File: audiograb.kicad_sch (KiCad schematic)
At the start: 8 parts, among them J2 USB_C_Receptacle_USB2.0_16P

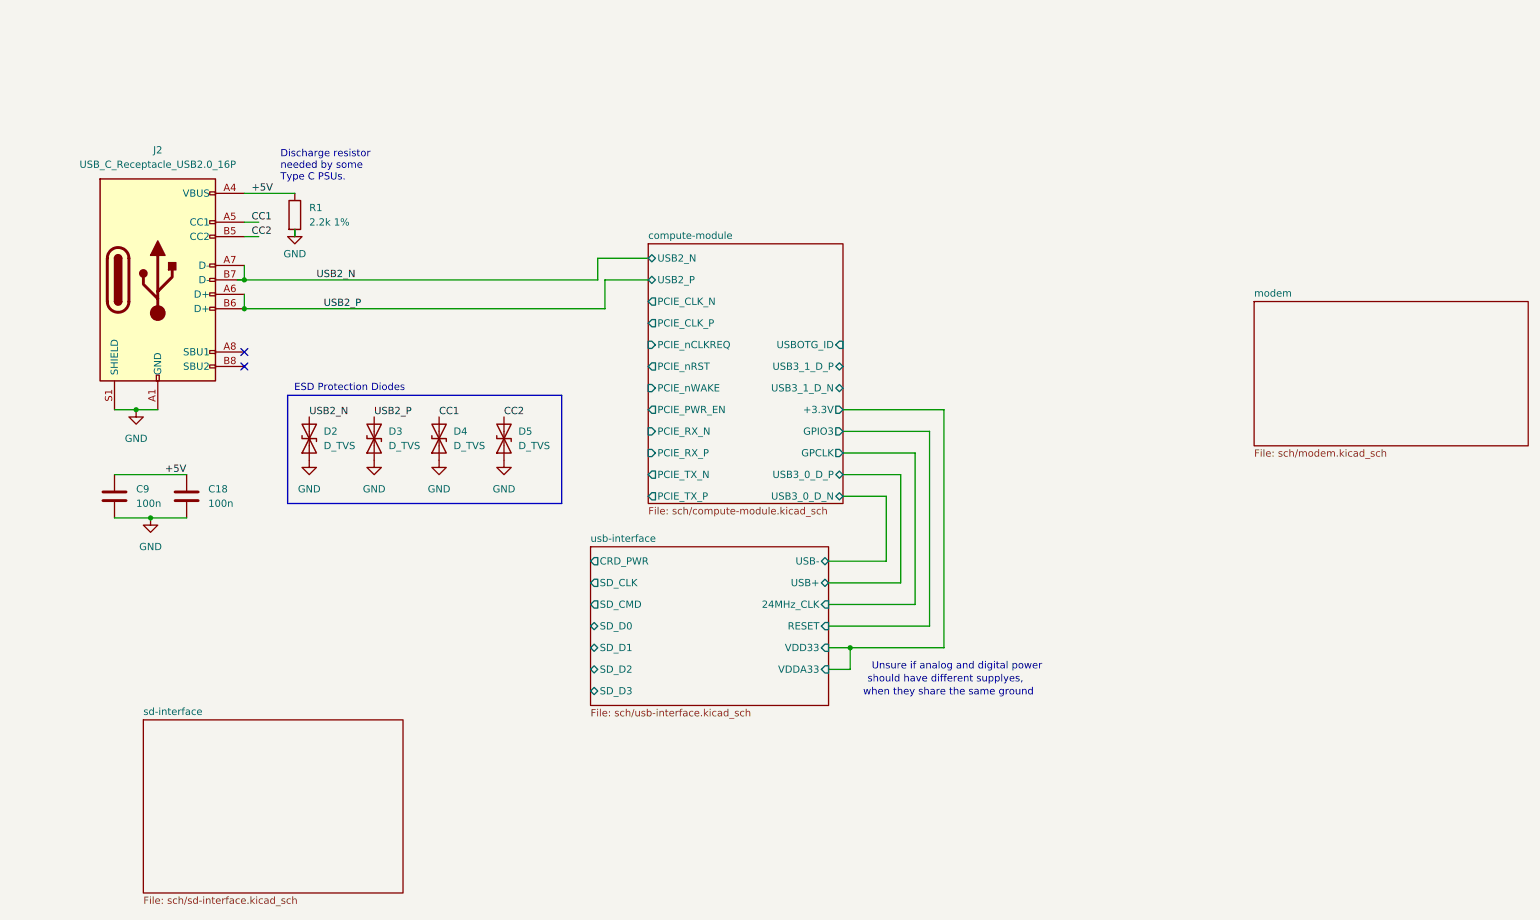
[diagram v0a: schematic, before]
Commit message: Connected pins between modem and CM5
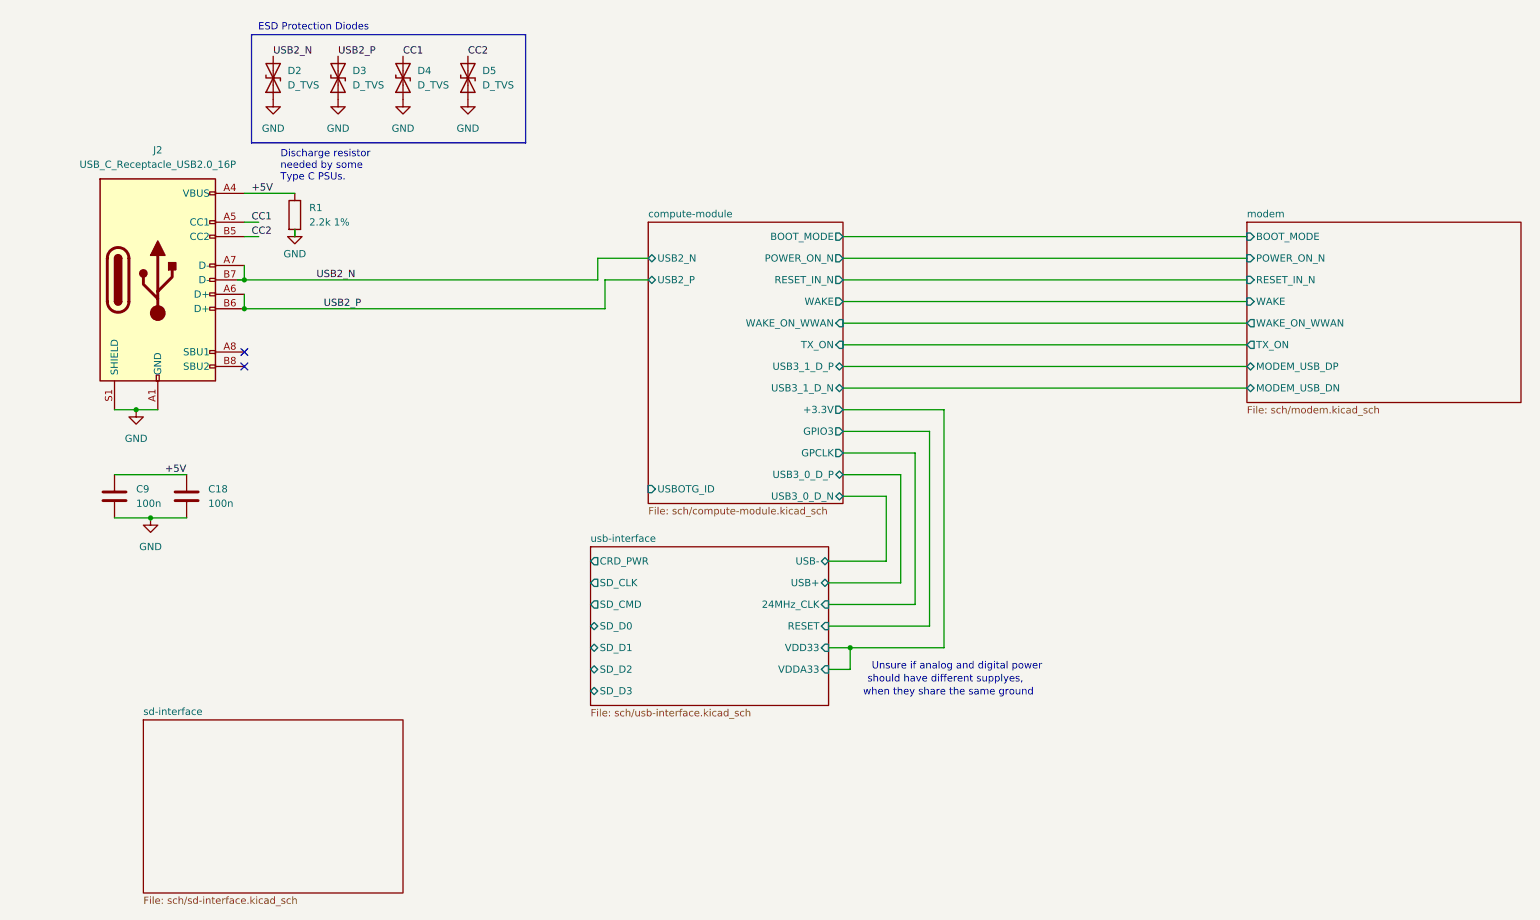
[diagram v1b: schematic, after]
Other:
- sheet compute-module ports: added BOOT_MODE, POWER_ON_N, RESET_IN_N, TX_ON, WAKE, WAKE_ON_WWAN; removed PCIE_CLK_N, PCIE_CLK_P, PCIE_PWR_EN, PCIE_RX_N, PCIE_RX_P, PCIE_TX_N, PCIE_TX_P, PCIE_nCLKREQ, PCIE_nRST, PCIE_nWAKE
- sheet modem ports: added BOOT_MODE, MODEM_USB_DN, MODEM_USB_DP, POWER_ON_N, RESET_IN_N, TX_ON, WAKE, WAKE_ON_WWAN; removed none
- moved on the sheet: D2, D3, D4, D5

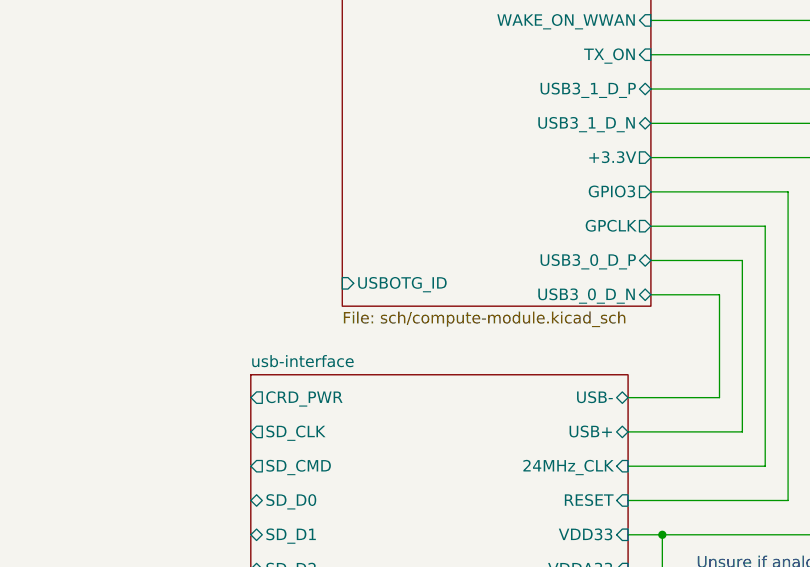
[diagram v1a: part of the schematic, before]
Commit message: Removed pin USBOTG
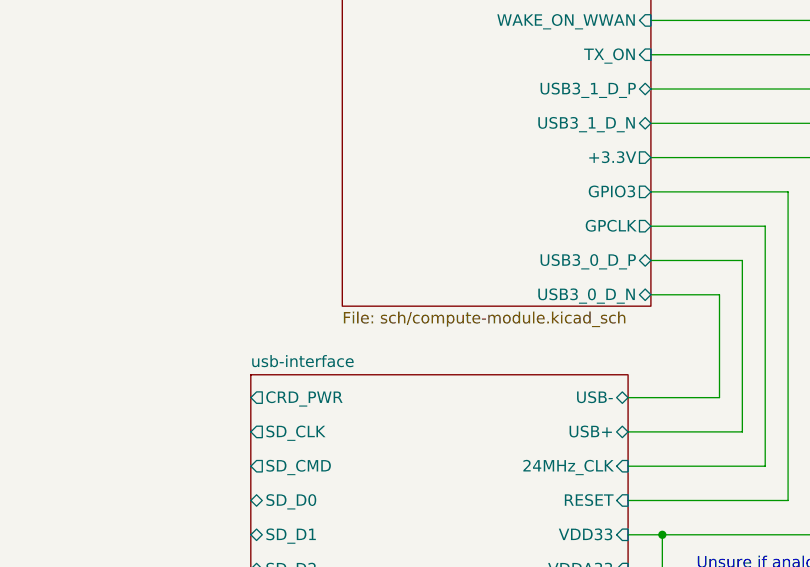
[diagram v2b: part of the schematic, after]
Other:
- sheet compute-module ports: added none; removed USBOTG_ID
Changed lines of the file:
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@@
-			)
-		)
-		(pin "USBOTG_ID" input
-			(at 123.19 96.52 180)
-			(effects
-				(font
-					(size 1.27 1.27)
-				)
-				(justify left)
 			)
 		)

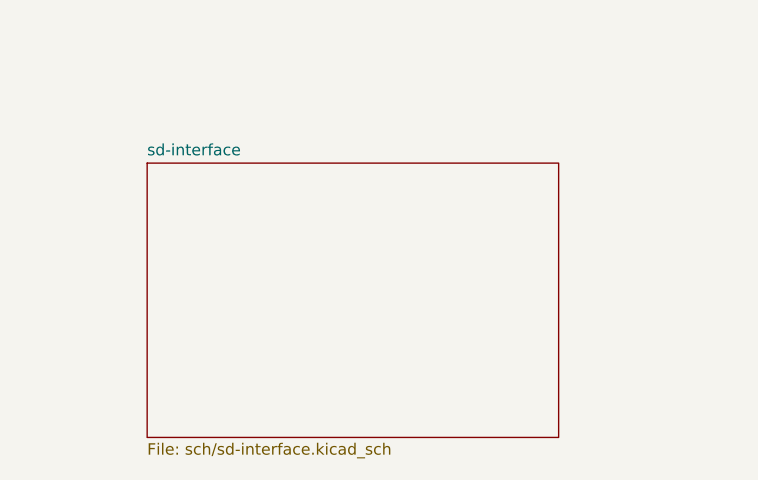
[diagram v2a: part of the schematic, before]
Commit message: added pins to sd_interface
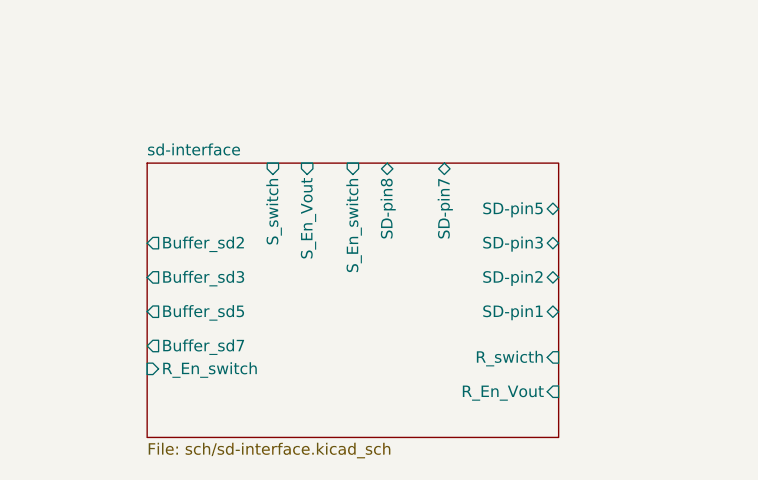
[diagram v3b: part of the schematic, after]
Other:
- sheet sd-interface ports: added Buffer_sd2, Buffer_sd3, Buffer_sd5, Buffer_sd7, R_En_Vout, R_En_switch, R_swicth, SD-pin1, SD-pin2, SD-pin3, SD-pin5, SD-pin7, SD-pin8, S_En_Vout, S_En_switch, S_switch; removed none
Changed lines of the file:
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@@
+			)
+		)
+		(pin "Buffer_sd2" output
+			(at 34.29 146.05 180)
+			(effects
+				(font
+					(size 1.27 1.27)
+				)
+				(justify left)
+			)
+		)
+		(pin "Buffer_sd3" output
+			(at 34.29 149.86 180)
+			(effects
+				(font
+					(size 1.27 1.27)
+				)
+				(justify left)
+			)
+		)
+		(pin "Buffer_sd5" output
+			(at 34.29 153.67 180)
+			(effects
+				(font
+					(size 1.27 1.27)
+				)
+				(justify left)
+			)
+		)
+		(pin "Buffer_sd7" output
+			(at 34.29 157.48 180)
+			(effects
+				(font
+					(size 1.27 1.27)
+				)
+				(justify left)
+			)
+		)
+		(pin "R_En_switch" input
+			(at 34.29 160.02 180)
+			(effects
+				(font
+					(size 1.27 1.27)
+				)
+				(justify left)
+			)
+		)
+		(pin "R_En_Vout" input
+			(at 80.01 162.56 0)
+			(effects
+				(font
+					(size 1.27 1.27)
+				)
+				(justify right)
+			)
+		)
+		(pin "R_swicth" input
+			(at 80.01 158.75 0)
+			(effects
+				(font
+					(size 1.27 1.27)
+				)
+				(justify right)
+			)
+		)
+		(pin "SD-pin1" bidirectional
+			(at 80.01 153.67 0)
+			(effects
+				(font
+					(size 1.27 1.27)
+				)
+				(justify right)
+			)
+		)
+		(pin "SD-pin2" bidirectional
+			(at 80.01 149.86 0)
+			(effects
+				(font
+					(size 1.27 1.27)
+				)
+				(justify right)
+			)
+		)
+		(pin "SD-pin3" bidirectional
+			(at 80.01 146.05 0)
+			(effects
+				(font
+					(size 1.27 1.27)
+				)
+				(justify right)
+			)
+		)
+		(pin "SD-pin5" bidirectional
+			(at 80.01 142.24 0)
+			(effects
+				(font
+					(size 1.27 1.27)
+				)
+				(justify right)
+			)
+		)
+		(pin "SD-pin7" bidirectional
+			(at 67.31 137.16 90)
+			(effects
+				(font
+					(size 1.27 1.27)
+				)
+				(justify right)
+			)
+		)
+		(pin "SD-pin8" bidirectional
+			(at 60.96 137.16 90)
+			(effects
+				(font
+					(size 1.27 1.27)
+				)
+				(justify right)
+			)
+		)
+		(pin "S_En_switch" input
+			(at 57.15 137.16 90)
+			(effects
+				(font
+					(size 1.27 1.27)
+				)
+				(justify right)
+			)
+		)
+		(pin "S_En_Vout" input
+			(at 52.07 137.16 90)
+			(effects
+				(font
+					(size 1.27 1.27)
+				)
+				(justify right)
+			)
+		)
+		(pin "S_switch" input
+			(at 48.26 137.16 90)
+			(effects
+				(font
+					(size 1.27 1.27)
+				)
+				(justify right)
 			)
 		)

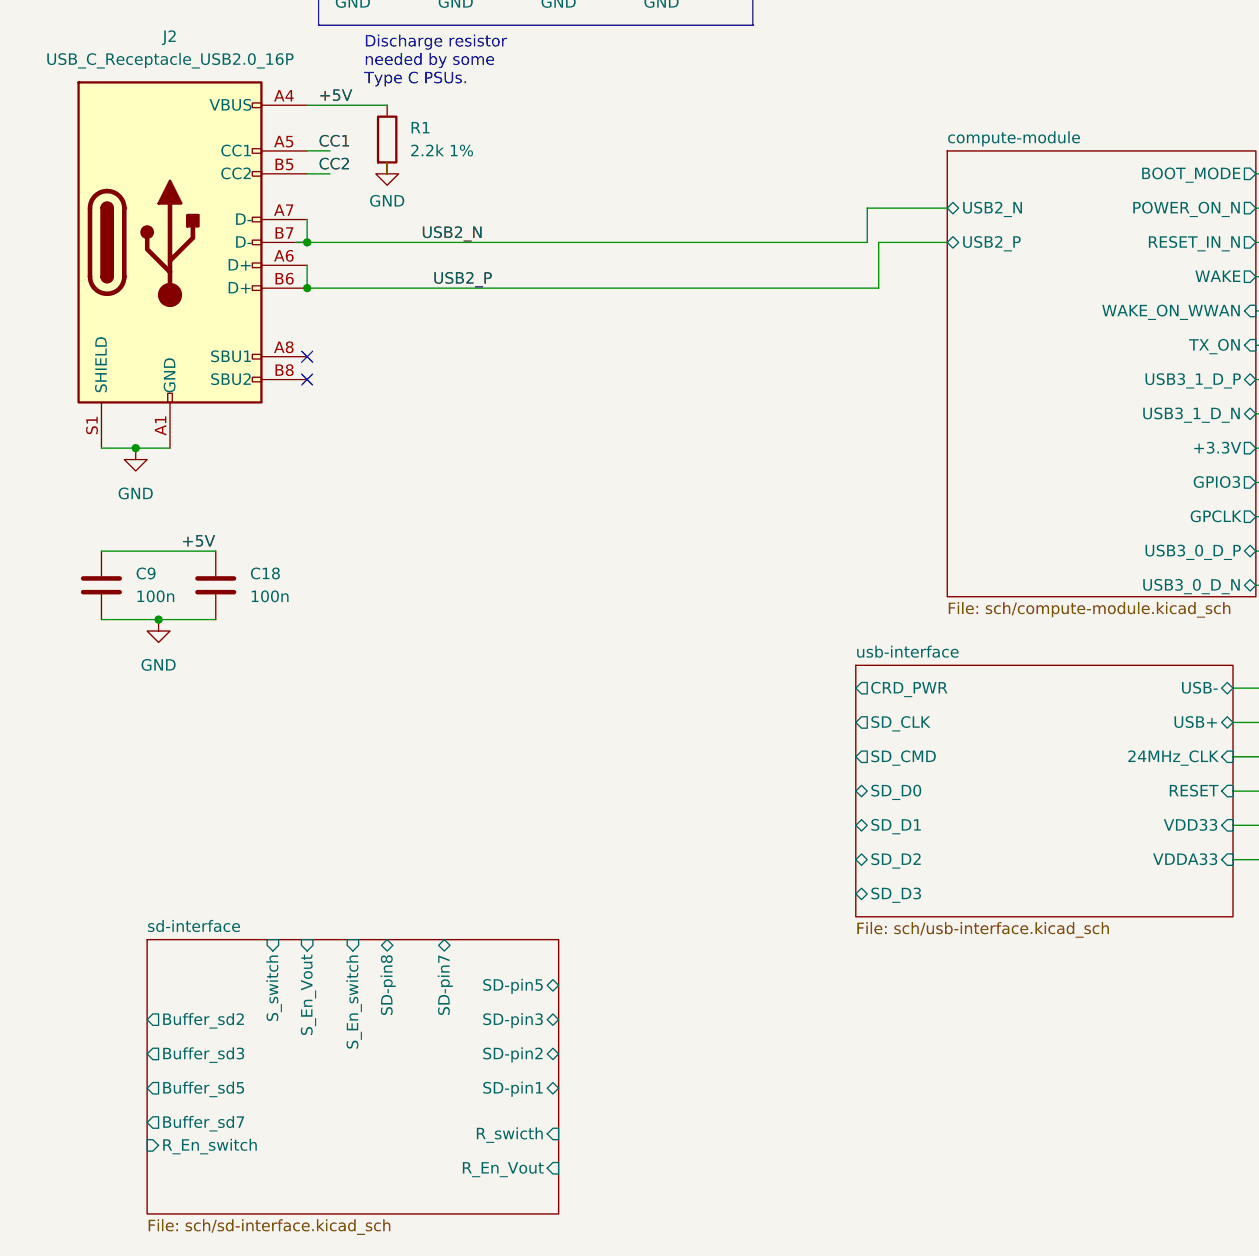
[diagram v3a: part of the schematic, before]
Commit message: All pins connected
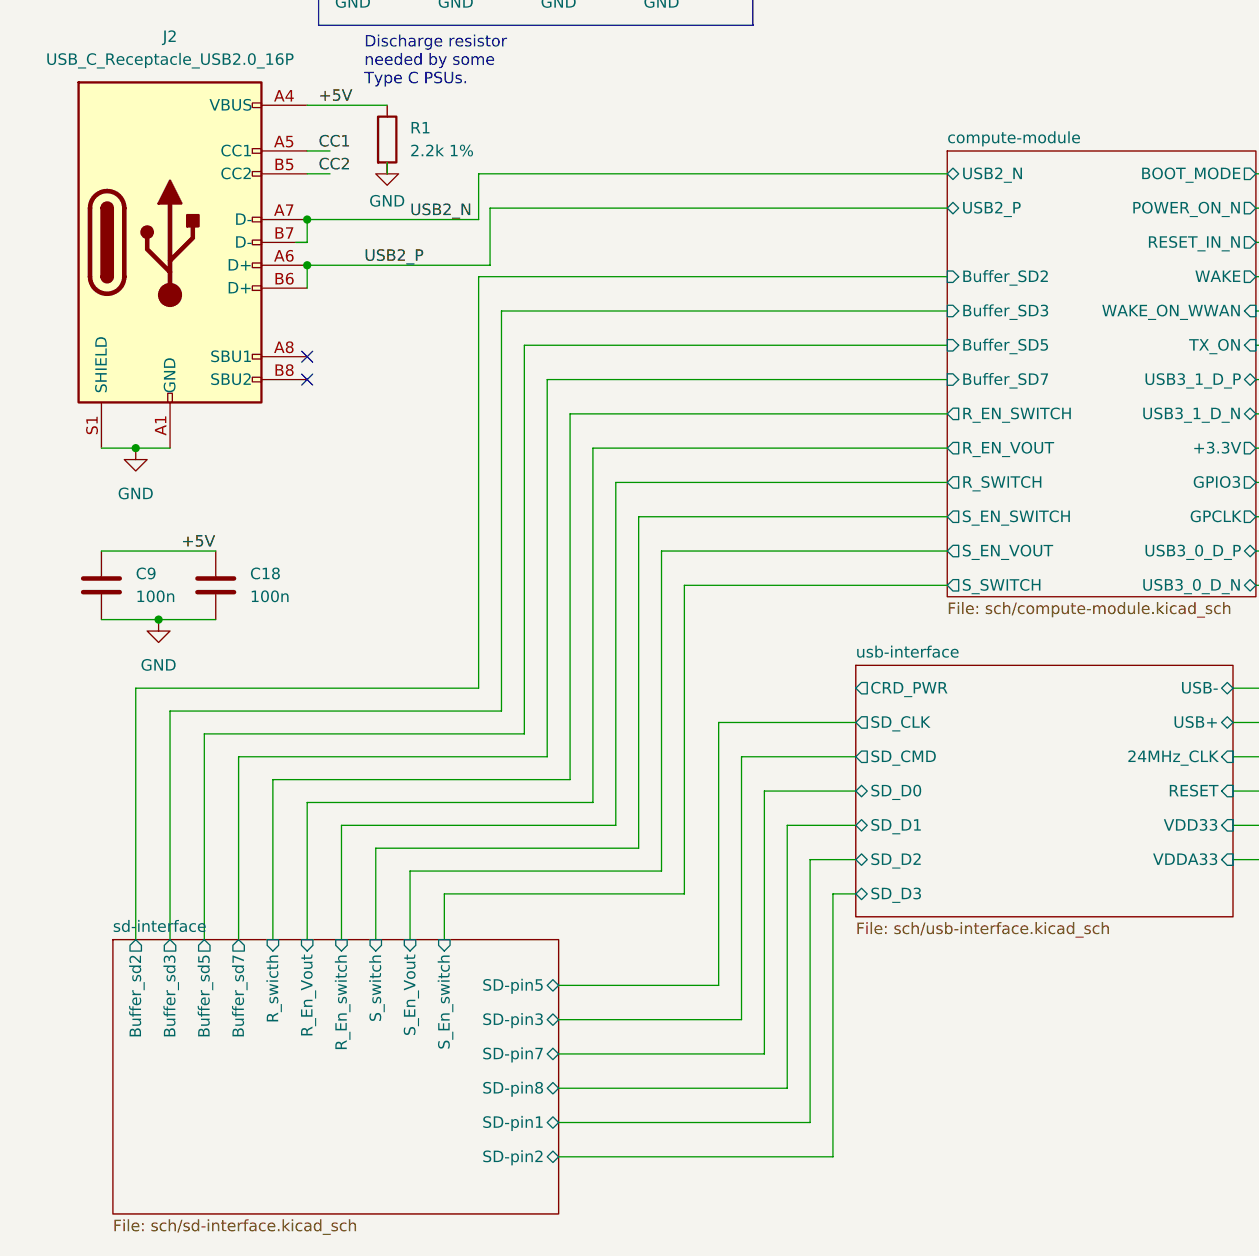
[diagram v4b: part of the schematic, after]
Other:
- sheet compute-module ports: added Buffer_SD2, Buffer_SD3, Buffer_SD5, Buffer_SD7, R_EN_SWITCH, R_EN_VOUT, R_SWITCH, S_EN_SWITCH, S_EN_VOUT, S_SWITCH; removed none
